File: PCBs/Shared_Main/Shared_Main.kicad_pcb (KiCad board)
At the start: 4 copper layers, 185.4 x 55.9 mm, 53 parts, among them J1 Power, J10 Digital inputs, J11 Digital inputs, J12 Digital inputs, J13 Digital inputs, J14 Digital inputs, J15 Digital inputs, J16 Other unit, J2 Rotary switches pin 1, J4 Aux, J5 Analog inputs, J7 Keypad, Q1 BC547, Q2 BC547, Q3 BC547, Q4 BC547, Q5 BC547, Q6 BC547, Q7 BC547, Q8 BC547, U1 ESP32-S3-ZERO, U2 74HC4051, U4 74HC165, U5 74HC165, U6 74HC165, U7 74HC165, U8 74HC165, U9 74HC165

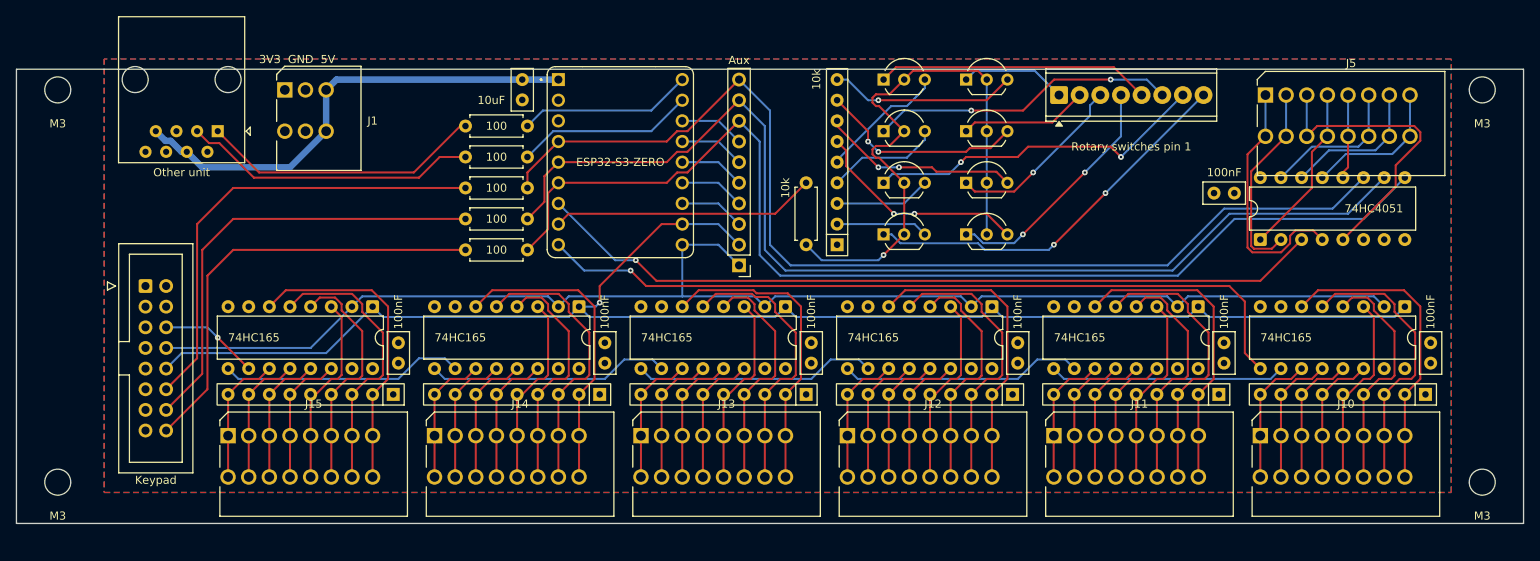
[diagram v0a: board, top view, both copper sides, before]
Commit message: reduce to 4 rotary switch pin-1s
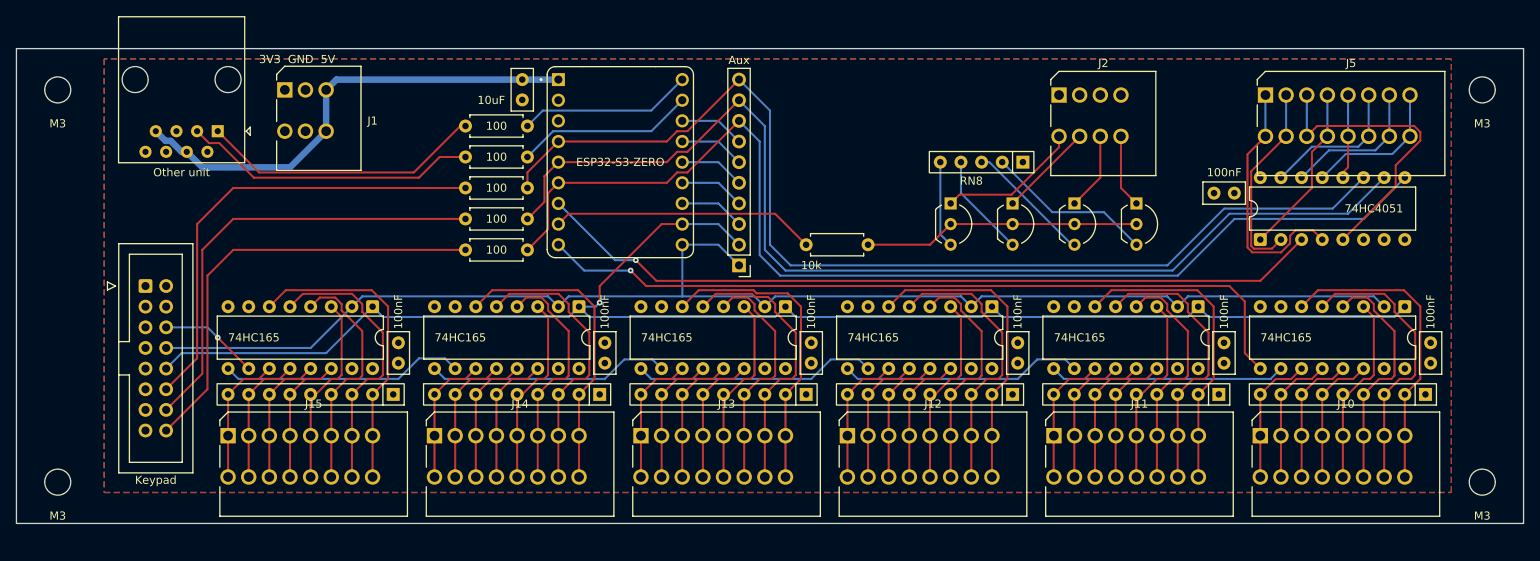
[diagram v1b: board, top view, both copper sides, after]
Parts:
- removed Q5, Q6, Q7, Q8: BC547, Package_TO_SOT_THT:TO-92_Inline_Wide
- J2: value Rotary switches pin 1 -> Screw_Terminal_01x04; footprint TerminalBlock_Phoenix:TerminalBlock_Phoenix_MPT-0,5-8-2.54_1x08_P2.54mm_Horizontal -> Custom_Footprints:SpringTerminal_1x04_P2.54mm_Vertical
- RN8: value 10k -> R_Network04; footprint Resistor_THT:R_Array_SIP9 -> Resistor_THT:R_Array_SIP5
- moved Q1 31.3 mm to (191.8, 82.5), turned to -90 degrees
- moved RN8 25.0 mm to (177.8, 77.5), turned to 180 degrees
- moved Q2 23.6 mm to (184.2, 82.5), turned to -90 degrees
- moved Q3 18.2 mm to (176.5, 82.5), turned to -90 degrees
- moved Q4 17.3 mm to (168.9, 82.5), turned to -90 degrees
- moved R1 7.62 mm to (158.8, 87.6), turned to 180 degrees
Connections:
- Q1 pad 1: Net-(J2-Pin_8) -> Net-(J2-Pin_4)
- Q2 pad 1: Net-(J2-Pin_7) -> Net-(J2-Pin_3)
- Q3 pad 1: Net-(J2-Pin_6) -> Net-(J2-Pin_2)
- Q4 pad 1: Net-(J2-Pin_5) -> Net-(J2-Pin_1)
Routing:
- net Net-(J2-Pin_8): track 48.0 -> 0.00 mm, vias 2 -> 0
- net Net-(J2-Pin_7): track 42.4 -> 0.00 mm, vias 2 -> 0
- net Net-(Q1-B): track 72.2 -> 34.1 mm, vias 1 -> 0
- net Net-(J2-Pin_6): track 37.7 -> 0.00 mm, vias 2 -> 0
- net Net-(J2-Pin_5): track 33.8 -> 0.00 mm
- net Net-(Q5-E): track 26.8 -> 0.00 mm, vias 2 -> 0
- net Net-(Q7-E): track 25.4 -> 0.00 mm, vias 2 -> 0
- net Net-(Q6-E): track 24.5 -> 0.00 mm, vias 2 -> 0
- net Net-(Q8-E): track 23.1 -> 0.00 mm, vias 1 -> 0
- net Net-(J2-Pin_4): track 30.0 -> 9.04 mm, vias 2 -> 0
- net Net-(J2-Pin_3): track 22.6 -> 9.57 mm, vias 1 -> 0
- net Net-(Q1-E): track 11.3 -> 20.7 mm
- net Net-(Q4-E): track 15.8 -> 10.7 mm
- net Net-(J2-Pin_1): track 13.1 -> 17.5 mm
- net Net-(J2-Pin_2): track 15.8 -> 11.7 mm
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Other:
- board size 185.4 x 55.9 mm -> 185.4 x 58.4 mm

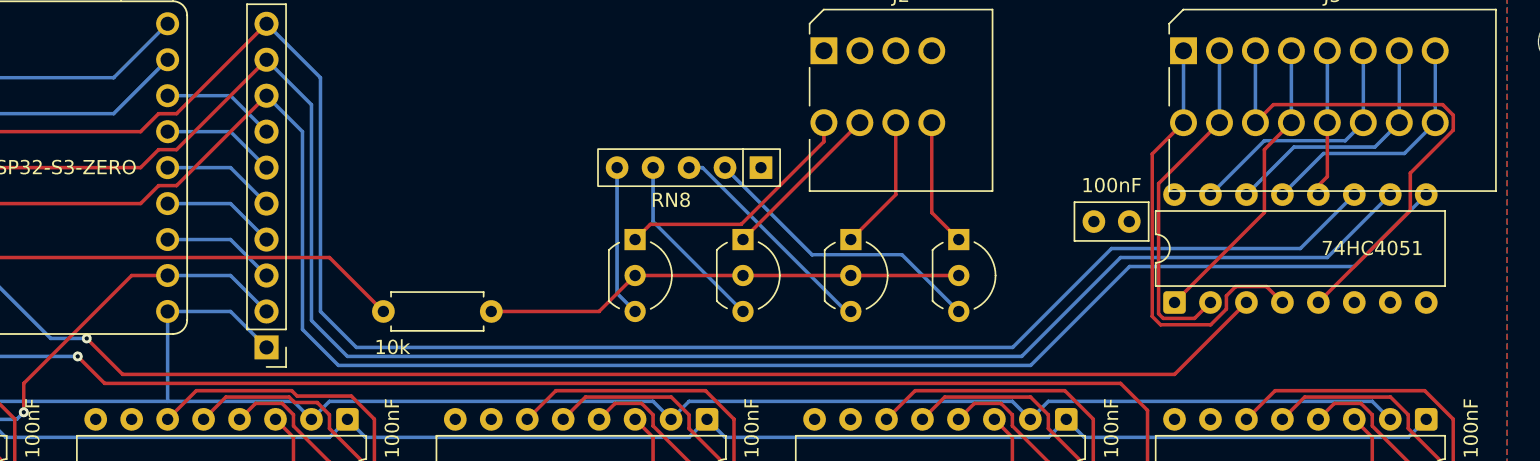
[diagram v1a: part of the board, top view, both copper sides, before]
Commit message: fix overlap
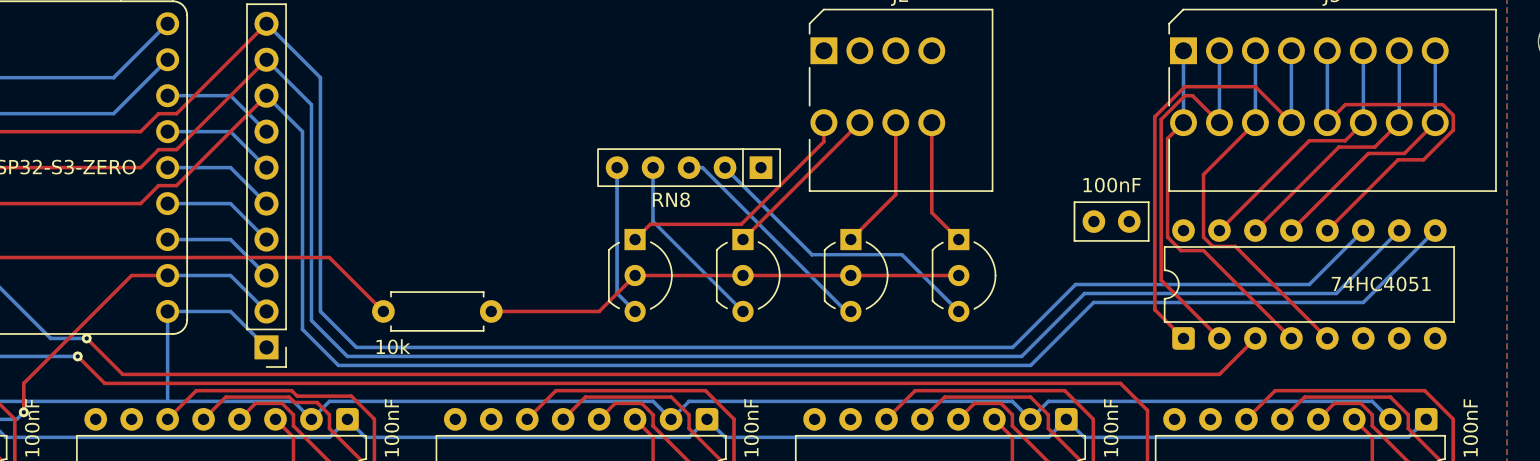
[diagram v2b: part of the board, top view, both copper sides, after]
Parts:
- moved U2 2.62 mm to (207.6, 89.5)
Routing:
- net Net-(J5-Pin_5): track 10.4 -> 27.7 mm
- net Net-(J5-Pin_4): track 21.2 -> 33.2 mm
- net Net-(J5-Pin_3): track 37.1 -> 26.4 mm
- net Net-(J5-Pin_1): track 31.2 -> 25.3 mm
- net Net-(J5-Pin_2): track 24.6 -> 27.9 mm

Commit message: reorganizing main pcb
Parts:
- moved J16 23.8 mm to (102.2, 77.5)
- moved J1 23.5 mm to (110.5, 68.6)
- moved C2 16.5 mm to (132.7, 69.8)
- moved R2 16.5 mm to (125.7, 76.8)
- moved R3 16.5 mm to (125.7, 73.0)
- moved R4 16.5 mm to (125.7, 80.6)
- moved R5 16.5 mm to (125.7, 84.5)
- moved R6 16.5 mm to (125.7, 88.3)
- moved J4 16.5 mm to (159.4, 90.2)
- moved U1 16.5 mm to (144.8, 77.5)
- moved R1 11.2 mm to (166.4, 79.4), turned to -90 degrees
- moved H3 10.2 mm to (69.2, 116.8)
- moved H4 10.2 mm to (69.2, 68.6)
- moved J7 5.08 mm to (69.8, 87.6)
- moved C1 2.65 mm to (203.2, 79.4), turned to -90 degrees
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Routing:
- net /ADDR2: track 137.8 -> 119.1 mm
- net /ADDR1: track 135.2 -> 116.7 mm
- net /ADDR0: track 132.7 -> 114.3 mm
- net /A: track 97.1 -> 79.5 mm
- net /SR_Q7: track 96.4 -> 79.5 mm, vias 1 -> 0
- net Net-(J16-FROM_B): track 36.7 -> 27.4 mm
- net Net-(J16-FROM_A): track 35.0 -> 26.0 mm
- net /ADDR2_KP: track 54.2 -> 62.9 mm
- net /SR_Q7_KP: track 12.3 -> 19.3 mm, vias 1 -> 0
- net /ADDR1_KP: track 55.5 -> 62.3 mm
- net /ADDR0_KP: track 56.8 -> 61.7 mm
- net +5V: track 58.8 -> 54.6 mm
- net Net-(Q1-B): track 34.1 -> 30.7 mm
- net /SR_CP: track 171.6 -> 175.0 mm
- net /ROT_PIN_1: track 32.6 -> 30.0 mm
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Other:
- board size 185.4 x 58.4 mm -> 175.3 x 58.4 mm

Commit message: wip
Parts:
- moved C2 0.64 mm to (133.3, 69.8)
- moved C1 0.63 mm to (202.6, 79.4)
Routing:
- net /A: track 79.5 -> 80.8 mm
- net /FROM_A: track 21.4 -> 21.9 mm
- net /SR_Q7: vias 0 -> 1
- net /ROT_PIN_1: vias 0 -> 2
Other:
- board size 175.3 x 58.4 mm -> 175.3 x 61 mm
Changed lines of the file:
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@@
 		(capping no)
 		(filling no)
+		(zone_defaults)
 		(pcbplotparams
 			(layerselection 0x00000000_00000000_55555555_5755f5ff)
@@
 	(footprint "Capacitor_THT:C_Disc_D5.0mm_W2.5mm_P2.50mm"
 		(layer "F.Cu")
-		(at 203.2 79.415 -90)
+		(at 202.565 79.415 -90)
 		(descr "C, Disc series, Radial, pin pitch=2.50mm, diameter*width=5*2.5mm^2, Capacitor, http://cdn-reichelt.de/documents/datenblatt/B300/DS_KERKO_TC.pdf")
 		(tags "C Disc series Radial pin pitch 2.50mm diameter 5mm width 2.5mm Capacitor")
@@
 	(footprint "Capacitor_THT:C_Disc_D5.0mm_W2.5mm_P2.50mm"
 		(layer "F.Cu")
-		(at 132.715 69.81 90)
+		(at 133.35 69.85 90)
 		(descr "C, Disc series, Radial, pin pitch=2.50mm, diameter*width=5*2.5mm^2, Capacitor, http://cdn-reichelt.de/documents/datenblatt/B300/DS_KERKO_TC.pdf")
 		(tags "C Disc series Radial pin pitch 2.50mm diameter 5mm width 2.5mm Capacitor")
@@
 	(gr_rect
 		(start 64.135 63.5)
-		(end 239.395 121.92)
+		(end 239.395 124.46)
 		(stroke
 			(width 0.05)
@@
 	)
 	(segment
-		(start 136.525 73.66)
-		(end 148.59 73.66)
+		(start 146.05 76.2)
+		(end 152.4 69.85)
 		(width 0.25)
 		(layer "B.Cu")
@@
 	)
 	(segment
-		(start 148.59 73.66)
-		(end 152.4 69.85)
+		(start 133.985 76.2)
+		(end 146.05 76.2)
 		(width 0.25)
 		(layer "B.Cu")
@@
 	(segment
 		(start 133.35 76.835)
-		(end 136.525 73.66)
+		(end 133.985 76.2)
 		(width 0.25)
 		(layer "B.Cu")
@@
 	)
 	(segment
-		(start 135.255 71.12)
-		(end 148.59 71.12)
+		(start 146.05 73.66)
+		(end 152.4 67.31)
 		(width 0.25)
 		(layer "B.Cu")
@@
 	)
 	(segment
-		(start 133.35 73.025)
-		(end 135.255 71.12)
+		(start 133.985 73.66)
+		(end 146.05 73.66)
 		(width 0.25)
 		(layer "B.Cu")
@@
 	)
 	(segment
-		(start 148.59 71.12)
-		(end 152.4 67.31)
+		(start 133.35 73.025)
+		(end 133.985 73.66)
 		(width 0.25)
 		(layer "B.Cu")
@@
 	(segment
 		(start 165.735 86.36)
-		(end 138.43 86.36)
+		(end 156.464 86.36)
 		(width 0.25)
 		(layer "F.Cu")
@@
 	)
 	(segment
-		(start 138.43 86.36)
-		(end 137.16 85.09)
+		(start 144.78 85.09)
+		(end 146.05 86.36)
 		(width 0.25)
 		(layer "F.Cu")
@@
 	)
 	(segment
+		(start 137.16 85.09)
+		(end 144.78 85.09)
+		(width 0.25)
+		(layer "F.Cu")
+		(net "/ROT_PIN_1")
+	)
+	(via
+		(at 146.05 86.36)
+		(size 0.7)
+		(drill 0.3)
+		(layers "F.Cu" "B.Cu")
+		(net "/ROT_PIN_1")
+	)
+	(via
+		(at 156.464 86.36)
+		(size 0.7)
+		(drill 0.3)
+		(layers "F.Cu" "B.Cu")
+		(net "/ROT_PIN_1")
+	)
+	(segment
+		(start 146.05 86.36)
+		(end 156.464 86.36)
+		(width 0.25)
+		(layer "B.Cu")
+		(net "/ROT_PIN_1")
+	)
+	(segment
 		(start 122.37 87.815)
 		(end 125.73 84.455)
@@
 	)
 	(segment
+		(start 154.527 93.377)
+		(end 154.686 93.377)
+		(width 0.25)
+		(layer "F.Cu")
+		(net "/SR_PL")
+	)
+	(segment
 		(start 152.654 95.25)
-		(end 154.686 93.218)
+		(end 154.527 93.377)
 		(width 0.25)
 		(layer "F.Cu")
@@
 	)
 	(via
-		(at 154.686 93.218)
+		(at 154.686 93.377)
 		(size 0.7)
 		(drill 0.3)
@@
 	)
 	(segment
+		(start 158.528 93.377)
+		(end 154.686 93.377)
+		(width 0.25)
+		(layer "B.Cu")
+		(net "/SR_PL")
+	)
+	(segment
 		(start 149.86 96.52)
 		(end 172.72 96.52)
@@
 	)
 	(segment
+		(start 160.56 88.805)
+		(end 160.56 91.345)
+		(width 0.25)
+		(layer "B.Cu")
+		(net "/SR_PL")
+	)
+	(segment
 		(start 156.845 85.09)
 		(end 159.385 87.63)
@@
 	)
 	(segment
-		(start 160.56 88.805)
-		(end 160.56 91.345)
-		(width 0.25)
-		(layer "B.Cu")
-		(net "/SR_PL")
-	)
-	(segment
-		(start 159.385 87.63)
-		(end 160.56 88.805)
+		(start 123.19 95.25)
+		(end 125.23 95.25)
 		(width 0.25)
 		(layer "B.Cu")
@@
 	)
 	(segment
-		(start 158.687 93.218)
-		(end 154.686 93.218)
+		(start 99.06 96.52)
+		(end 121.92 96.52)
 		(width 0.25)
 		(layer "B.Cu")
@@
 	)
 	(segment
-		(start 123.19 95.25)
-		(end 125.23 95.25)
+		(start 160.56 91.345)
+		(end 158.528 93.377)
 		(width 0.25)
 		(layer "B.Cu")
@@
 	)
 	(segment
-		(start 99.06 96.52)
-		(end 121.92 96.52)
+		(start 124.46 96.52)
+		(end 147.32 96.52)
 		(width 0.25)
 		(layer "B.Cu")
@@
 	)
 	(segment
-		(start 124.46 96.52)
-		(end 147.32 96.52)
+		(start 159.385 87.63)
+		(end 160.56 88.805)
 		(width 0.25)
 		(layer "B.Cu")
@@
 	)
 	(segment
-		(start 160.56 91.345)
-		(end 158.687 93.218)
+		(start 135.89 93.98)
+		(end 144.78 93.98)
 		(width 0.25)
 		(layer "B.Cu")
-		(net "/SR_PL")
+		(net "/SR_CP")
 	)
 	(segment
-		(start 146.05 95.25)
-		(end 147.32 93.98)
+		(start 170.302 94.102)
+		(end 171.45 95.25)
 		(width 0.25)
 		(layer "B.Cu")
@@
 	)
 	(segment
-		(start 135.89 93.98)
-		(end 144.78 93.98)
+		(start 147.198 94.102)
+		(end 170.302 94.102)
 		(width 0.25)
 		(layer "B.Cu")
@@
 	)
 	(segment
-		(start 147.32 93.98)
-		(end 170.18 93.98)
-		(width 0.25)
-		(layer "B.Cu")
-		(net "/SR_CP")
-	)
-	(segment
 		(start 152.4 88.9)
 		(end 146.05 95.25)
@@
 	)
 	(segment
-		(start 170.18 93.98)
-		(end 171.45 95.25)
+		(start 95.25 95.25)
+		(end 93.345 97.155)
 		(width 0.25)
 		(layer "B.Cu")
@@
 	)
 	(segment
-		(start 95.25 95.25)
-		(end 93.345 97.155)
+		(start 146.05 95.25)
+		(end 147.198 94.102)
 		(width 0.25)
 		(layer "B.Cu")
@@
 	)
 	(segment
-		(start 212.09 89.662)
-		(end 210.312 91.44)
+		(start 212.09 89.535)
+		(end 209.423 92.202)
 		(width 0.25)
 		(layer "F.Cu")
@@
 	)
 	(segment
-		(start 212.09 89.535)
-		(end 212.09 89.662)
+		(start 209.423 92.202)
+		(end 145.542 92.202)
 		(width 0.25)
 		(layer "F.Cu")
@@
 	)
 	(segment
-		(start 210.312 91.44)
-		(end 148.59 91.44)
+		(start 145.542 92.202)
+		(end 143.637 90.297)
 		(width 0.25)
 		(layer "F.Cu")
@@
 	)
 	(via
-		(at 148.59 91.44)
+		(at 143.637 90.297)
 		(size 0.7)
 		(drill 0.3)
@@
 	)
 	(segment
-		(start 148.59 91.44)
-		(end 139.7 82.55)
+		(start 137.16 82.55)
+		(end 143.637 89.027)
 		(width 0.25)
 		(layer "B.Cu")
@@
 	)
 	(segment
-		(start 139.7 82.55)
-		(end 137.16 82.55)
+		(start 143.637 89.027)
+		(end 143.637 90.297)
 		(width 0.25)
 		(layer "B.Cu")
@@
 	)
 	(segment
-		(start 202.348 92.493)
+		(start 207.01 102.87)
 		(end 207.01 97.155)
 		(width 0.25)
@@
 	)
 	(segment
-		(start 142.023 92.493)
-		(end 202.348 92.493)
+		(start 207.01 97.155)
+		(end 202.507 92.652)
 		(width 0.25)
 		(layer "F.Cu")
@@
 	)
 	(segment
-		(start 137.16 87.63)
-		(end 142.023 92.493)
+		(start 202.507 92.652)
+		(end 142.182 92.652)
 		(width 0.25)
 		(layer "F.Cu")
@@
 	)
 	(segment
-		(start 207.01 97.155)
-		(end 207.01 102.87)
+		(start 142.182 92.652)
+		(end 139.827 90.297)
 		(width 0.25)
 		(layer "F.Cu")
 		(net "/SR_Q7")
 	)
+	(via
+		(at 139.827 90.297)
+		(size 0.7)
+		(drill 0.3)
+		(layers "F.Cu" "B.Cu")
+		(net "/SR_Q7")
+	)
+	(segment
+		(start 137.16 87.63)
+		(end 139.827 90.297)
+		(width 0.25)
+		(layer "B.Cu")
+		(net "/SR_Q7")
+	)
 	(segment
 		(start 105.41 102.87)
@@
 		(polygon
 			(pts
-				(xy 64.77 64.77) (xy 64.77 118.11) (xy 230.505 118.11) (xy 230.505 64.77)
+				(xy 64.77 64.77) (xy 64.77 112.395) (xy 73.66 112.395) (xy 73.66 120.142) (xy 230.505 120.142) (xy 230.505 64.77)
 			)
 		)
@@
 		(polygon
 			(pts
-				(xy 64.77 64.77) (xy 64.77 118.11) (xy 230.505 118.11) (xy 230.505 64.77)
+				(xy 64.77 64.77) (xy 64.77 112.395) (xy 73.66 112.395) (xy 73.66 120.142) (xy 230.505 120.142) (xy 230.505 64.77)
 			)
 		)
@@
 		(polygon
 			(pts
-				(xy 64.77 118.11) (xy 230.505 118.11) (xy 230.505 64.77) (xy 64.77 64.77)
+				(xy 64.77 120.142) (xy 230.505 120.142) (xy 230.505 64.77) (xy 64.77 64.77)
 			)
 		)
@@
 		(polygon
 			(pts
-				(xy 64.77 118.11) (xy 230.505 118.11) (xy 230.505 64.77) (xy 64.77 64.77)
+				(xy 64.77 120.142) (xy 230.505 120.142) (xy 230.505 64.77) (xy 64.77 64.77)
 			)
 		)
